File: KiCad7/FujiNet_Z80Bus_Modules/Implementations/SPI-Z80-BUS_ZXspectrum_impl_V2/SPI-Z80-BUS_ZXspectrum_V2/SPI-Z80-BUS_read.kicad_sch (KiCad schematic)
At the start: 4 parts

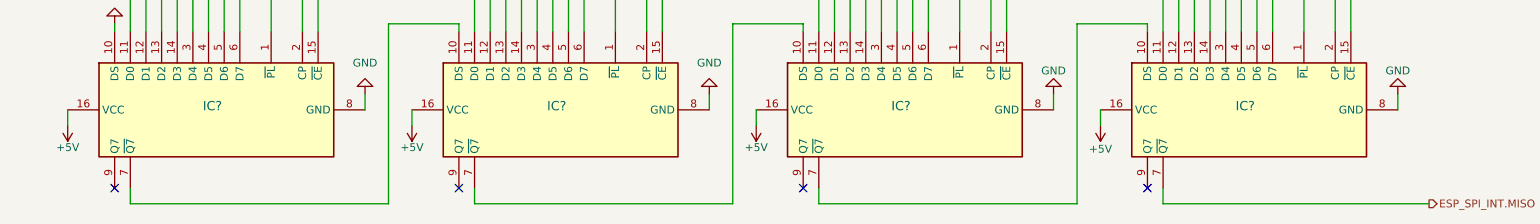
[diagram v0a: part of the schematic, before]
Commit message: KICAD - Restructure and SPI version2 Draft
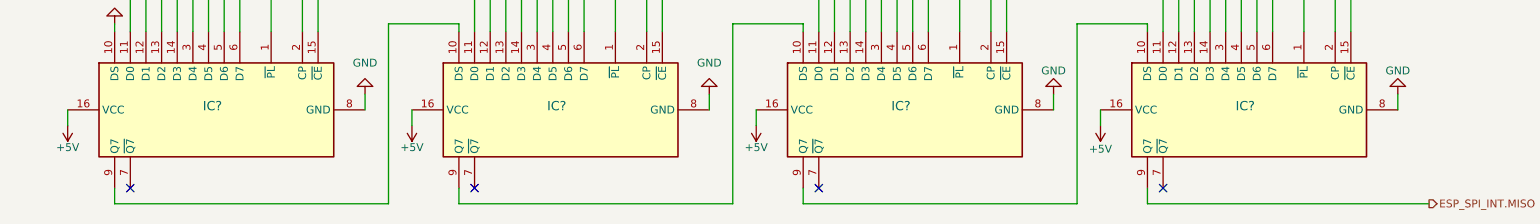
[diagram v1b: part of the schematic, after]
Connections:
- net ESP_SPI_INT.MISO: now also IC?.9 (Q7); no longer IC?.7 (~{Q7})
- net at IC?.10 (DS): now also IC?.9 (Q7); no longer IC?.7 (~{Q7}) (x2)
- net at IC?.7 (~{Q7}): no longer IC?.10 (DS)
- net at IC?.9 (Q7): now also IC?.10 (DS)
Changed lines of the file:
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@@
 (kicad_sch (version 20230121) (generator eeschema)
   (paper "A4")
-  (no_connect (at 212.09 115.57))
-  (no_connect (at 44.45 115.57))
-  (no_connect (at 156.21 115.57))
-  (no_connect (at 100.33 115.57))
+  (no_connect (at 214.63 115.57))
+  (no_connect (at 158.75 115.57))
+  (no_connect (at 46.99 115.57))
+  (no_connect (at 102.87 115.57))
   (bus_entry (at 52.07 60.96) (size 2.54 2.54)
     (stroke (width 0) (type default))
@@
     (stroke (width 0) (type default))
   )
-  (wire (pts (xy 46.99 115.57) (xy 46.99 118.11))
+  (wire (pts (xy 44.45 115.57) (xy 44.45 118.11))
     (stroke (width 0) (type default))
   )
@@
     (stroke (width 0) (type default))
   )
-  (wire (pts (xy 46.99 118.11) (xy 88.9 118.11))
+  (wire (pts (xy 44.45 118.11) (xy 88.9 118.11))
     (stroke (width 0) (type default))
   )
@@
     (stroke (width 0) (type default))
   )
-  (wire (pts (xy 257.81 118.11) (xy 214.63 118.11))
+  (wire (pts (xy 212.09 118.11) (xy 257.81 118.11))
     (stroke (width 0) (type default))
   )
@@
     (stroke (width 0) (type default))
   )
-  (wire (pts (xy 102.87 118.11) (xy 144.78 118.11))
+  (wire (pts (xy 100.33 118.11) (xy 144.78 118.11))
     (stroke (width 0) (type default))
   )
@@
     (stroke (width 0) (type default))
   )
-  (wire (pts (xy 214.63 118.11) (xy 214.63 115.57))
+  (wire (pts (xy 212.09 118.11) (xy 212.09 115.57))
     (stroke (width 0) (type default))
   )
@@
     (stroke (width 0) (type default))
   )
-  (wire (pts (xy 158.75 118.11) (xy 200.66 118.11))
+  (wire (pts (xy 156.21 118.11) (xy 200.66 118.11))
     (stroke (width 0) (type default))
   )
@@
     (stroke (width 0) (type default))
   )
-  (wire (pts (xy 158.75 118.11) (xy 158.75 115.57))
+  (wire (pts (xy 156.21 118.11) (xy 156.21 115.57))
     (stroke (width 0) (type default))
   )
@@
     (stroke (width 0) (type default))
   )
-  (wire (pts (xy 102.87 115.57) (xy 102.87 118.11))
+  (wire (pts (xy 100.33 115.57) (xy 100.33 118.11))
     (stroke (width 0) (type default))
   )
@@
         )
       )
-      (project "SPI-Z80-BUS_ZXspectrum_impl"
+      (project "SPI-Z80-BUS-ZXSpectrum_impl_V2"
         (path "/532c0392-800e-45cc-8170-6d32f2390e83/9a993edb-7f20-4cca-a657-2a2140304b51/28782bf7-67b4-4359-a03a-a82310c7ca9d"
           (reference "#PWR013") (unit 1)
@@
         )
       )
-      (project "SPI-Z80-BUS_ZXspectrum_impl"
+      (project "SPI-Z80-BUS-ZXSpectrum_impl_V2"
         (path "/532c0392-800e-45cc-8170-6d32f2390e83/9a993edb-7f20-4cca-a657-2a2140304b51/28782bf7-67b4-4359-a03a-a82310c7ca9d"
           (reference "#PWR016") (unit 1)
@@
         )
       )
-      (project "SPI-Z80-BUS_ZXspectrum_impl"
+      (project "SPI-Z80-BUS-ZXSpectrum_impl_V2"
         (path "/532c0392-800e-45cc-8170-6d32f2390e83"
           (reference "IC?") (unit 1)
@@
         )
       )
-      (project "SPI-Z80-BUS_ZXspectrum_impl"
+      (project "SPI-Z80-BUS-ZXSpectrum_impl_V2"
         (path "/532c0392-800e-45cc-8170-6d32f2390e83/9a993edb-7f20-4cca-a657-2a2140304b51/28782bf7-67b4-4359-a03a-a82310c7ca9d"
           (reference "#PWR017") (unit 1)
@@
         )
       )
-      (project "SPI-Z80-BUS_ZXspectrum_impl"
+      (project "SPI-Z80-BUS-ZXSpectrum_impl_V2"
         (path "/532c0392-800e-45cc-8170-6d32f2390e83/9a993edb-7f20-4cca-a657-2a2140304b51/28782bf7-67b4-4359-a03a-a82310c7ca9d"
           (reference "#PWR020") (unit 1)
@@
         )
       )
-      (project "SPI-Z80-BUS_ZXspectrum_impl"
+      (project "SPI-Z80-BUS-ZXSpectrum_impl_V2"
         (path "/532c0392-800e-45cc-8170-6d32f2390e83/9a993edb-7f20-4cca-a657-2a2140304b51/28782bf7-67b4-4359-a03a-a82310c7ca9d"
           (reference "#PWR015") (unit 1)
@@
         )
       )
-      (project "SPI-Z80-BUS_ZXspectrum_impl"
+      (project "SPI-Z80-BUS-ZXSpectrum_impl_V2"
         (path "/532c0392-800e-45cc-8170-6d32f2390e83"
           (reference "IC?") (unit 1)
@@
         )
       )
-      (project "SPI-Z80-BUS_ZXspectrum_impl"
+      (project "SPI-Z80-BUS-ZXSpectrum_impl_V2"
         (path "/532c0392-800e-45cc-8170-6d32f2390e83/9a993edb-7f20-4cca-a657-2a2140304b51/28782bf7-67b4-4359-a03a-a82310c7ca9d"
           (reference "#PWR014") (unit 1)
@@
         )
       )
-      (project "SPI-Z80-BUS_ZXspectrum_impl"
+      (project "SPI-Z80-BUS-ZXSpectrum_impl_V2"
         (path "/532c0392-800e-45cc-8170-6d32f2390e83"
           (reference "IC?") (unit 1)
@@
         )
       )
-      (project "SPI-Z80-BUS_ZXspectrum_impl"
+      (project "SPI-Z80-BUS-ZXSpectrum_impl_V2"
         (path "/532c0392-800e-45cc-8170-6d32f2390e83/9a993edb-7f20-4cca-a657-2a2140304b51/28782bf7-67b4-4359-a03a-a82310c7ca9d"
           (reference "#PWR018") (unit 1)
@@
         )
       )
-      (project "SPI-Z80-BUS_ZXspectrum_impl"
+      (project "SPI-Z80-BUS-ZXSpectrum_impl_V2"
         (path "/532c0392-800e-45cc-8170-6d32f2390e83"
           (reference "IC?") (unit 1)
@@
         )
       )
-      (project "SPI-Z80-BUS_ZXspectrum_impl"
+      (project "SPI-Z80-BUS-ZXSpectrum_impl_V2"
         (path "/532c0392-800e-45cc-8170-6d32f2390e83/9a993edb-7f20-4cca-a657-2a2140304b51/28782bf7-67b4-4359-a03a-a82310c7ca9d"
           (reference "#PWR019") (unit 1)
@@
         )
       )
-      (project "SPI-Z80-BUS_ZXspectrum_impl"
+      (project "SPI-Z80-BUS-ZXSpectrum_impl_V2"
         (path "/532c0392-800e-45cc-8170-6d32f2390e83/9a993edb-7f20-4cca-a657-2a2140304b51/28782bf7-67b4-4359-a03a-a82310c7ca9d"
           (reference "#PWR021") (unit 1)
